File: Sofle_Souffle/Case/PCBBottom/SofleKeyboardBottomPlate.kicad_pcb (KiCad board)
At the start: 2 copper layers, 143.4 x 111.8 mm, 15 parts

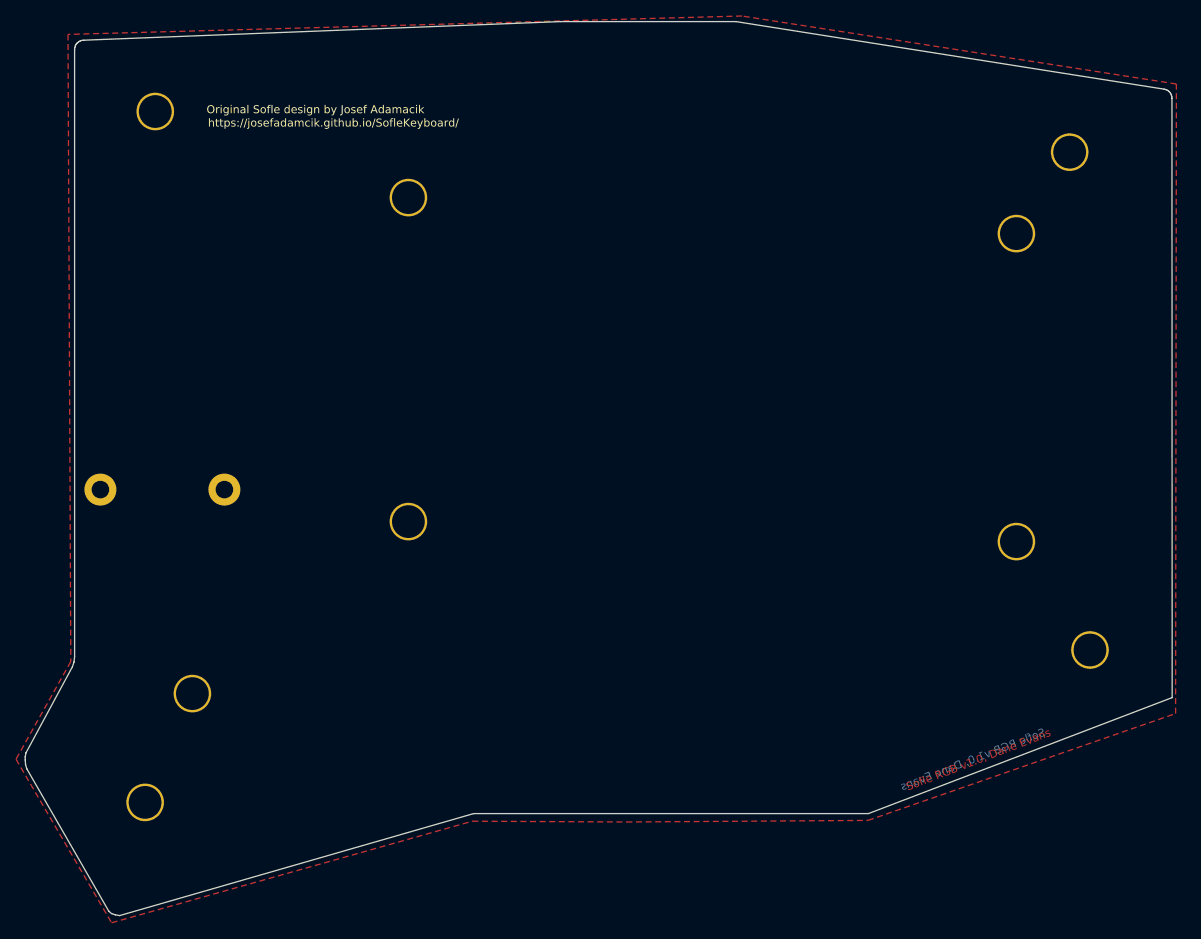
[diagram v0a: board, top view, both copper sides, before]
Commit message: Updated bottom plate and added SVG files for case creation.
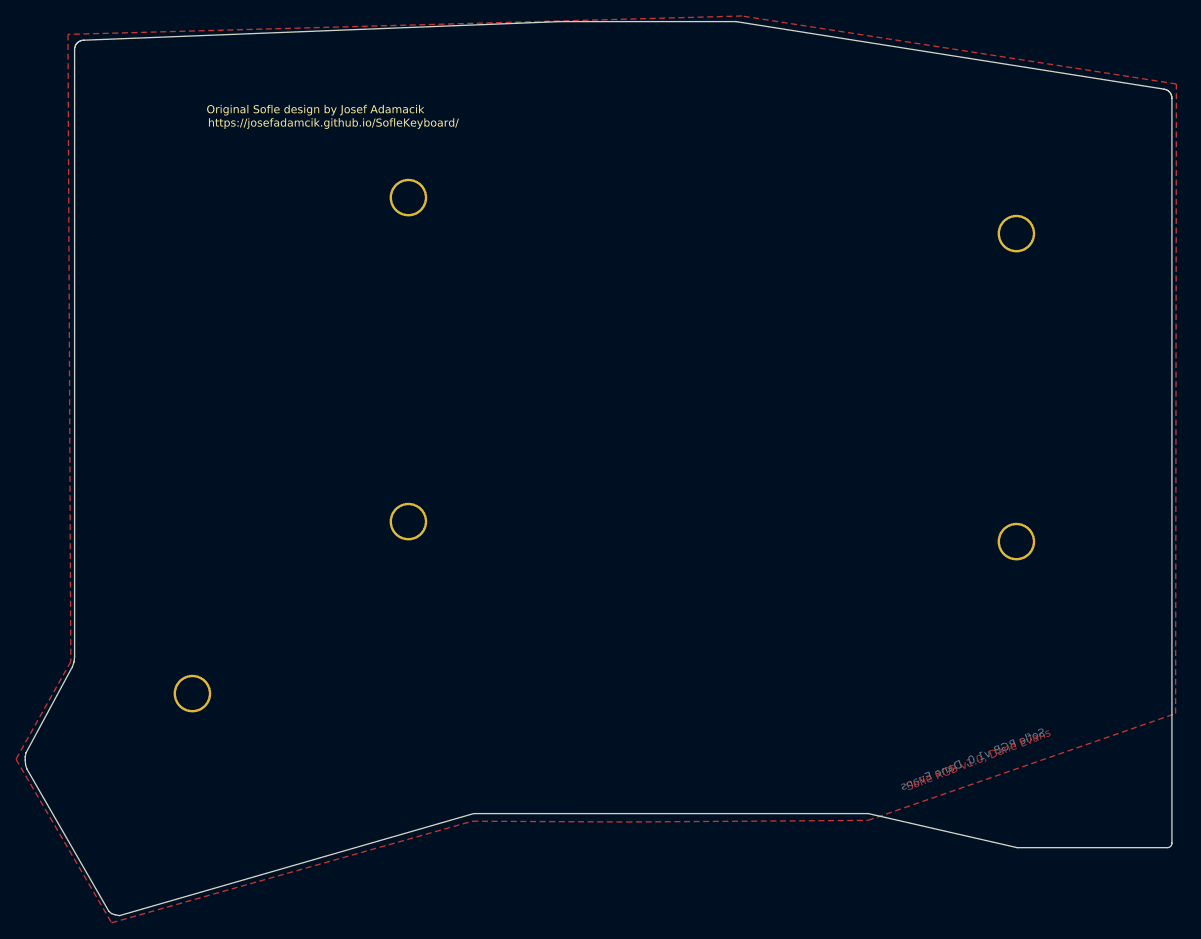
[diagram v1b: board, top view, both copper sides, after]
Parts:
- removed TH1, TH2: HOLE, SofleKeyboard-footprint:M2_HOLE_PCB
- removed the TH3 at (215.9, 114.3)
- removed the TH3 at (213.4, 52.1)
- removed the TH3 at (97.8, 133.3)
- removed the TH3 at (99.1, 47.0)
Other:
- board size 143.4 x 111.8 mm -> 143.3 x 111.8 mm
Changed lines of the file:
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@@
-(kicad_pcb (version 20171130) (host pcbnew "(5.1.6)-1")
+(kicad_pcb (version 20171130) (host pcbnew "(5.1.12-1-10_14)")
   (general
     (thickness 1.6)
-    (drawings 41)
+    (drawings 44)
     (tracks 0)
     (zones 0)
-    (modules 15)
+    (modules 9)
     (nets 1)
   )
@@
     (38 B.Mask user)
     (39 F.Mask user)
-    (40 Dwgs.User user hide)
+    (40 Dwgs.User user)
     (41 Cmts.User user hide)
     (42 Eco1.User user hide)
@@
   )
   (module SofleKeyboard-footprint:HOLE_M2_TH (layer F.Cu)
-    (at 215.9 114.3)
-    (fp_text reference TH3 (at 0 -2.54) (layer F.SilkS) hide
-      (effects (font (size 0.29972 0.29972) (thickness 0.0762)))
-    )
-    (fp_text value HOLE (at 0 2.54) (layer F.SilkS) hide
-      (effects (font (size 0.29972 0.29972) (thickness 0.0762)))
-    )
-    (pad "" thru_hole circle (at 0.025 -0.075 90) (size 4.7 4.7) (drill 4.1) (layers *.Cu *.Mask Dwgs.User)
-      (clearance 0.3))
-  )
-  (module SofleKeyboard-footprint:HOLE_M2_TH (layer F.Cu)
-    (at 213.36 52.07)
-    (fp_text reference TH3 (at 0 -2.54) (layer F.SilkS) hide
-      (effects (font (size 0.29972 0.29972) (thickness 0.0762)))
-    )
-    (fp_text value HOLE (at 0 2.54) (layer F.SilkS) hide
-      (effects (font (size 0.29972 0.29972) (thickness 0.0762)))
-    )
-    (pad "" thru_hole circle (at 0.025 -0.075 90) (size 4.7 4.7) (drill 4.1) (layers *.Cu *.Mask Dwgs.User)
-      (clearance 0.3))
-  )
-  (module SofleKeyboard-footprint:HOLE_M2_TH (layer F.Cu)
-    (at 97.79 133.35)
-    (fp_text reference TH3 (at 0 -2.54) (layer F.SilkS) hide
-      (effects (font (size 0.29972 0.29972) (thickness 0.0762)))
-    )
-    (fp_text value HOLE (at 0 2.54) (layer F.SilkS) hide
-      (effects (font (size 0.29972 0.29972) (thickness 0.0762)))
-    )
-    (pad "" thru_hole circle (at 0.025 -0.075 90) (size 4.7 4.7) (drill 4.1) (layers *.Cu *.Mask Dwgs.User)
-      (clearance 0.3))
-  )
-  (module SofleKeyboard-footprint:HOLE_M2_TH (layer F.Cu)
-    (at 99.06 46.99)
-    (fp_text reference TH3 (at 0 -2.54) (layer F.SilkS) hide
-      (effects (font (size 0.29972 0.29972) (thickness 0.0762)))
-    )
-    (fp_text value HOLE (at 0 2.54) (layer F.SilkS) hide
-      (effects (font (size 0.29972 0.29972) (thickness 0.0762)))
-    )
-    (pad "" thru_hole circle (at 0.025 -0.075 90) (size 4.7 4.7) (drill 4.1) (layers *.Cu *.Mask Dwgs.User)
-      (clearance 0.3))
-  )
-  (module SofleKeyboard-footprint:M2_HOLE_PCB (layer F.Cu)
-    (at 92.225 94.175)
-    (fp_text reference TH1 (at 0 2.7) (layer F.SilkS) hide
-      (effects (font (size 1 1) (thickness 0.15)))
-    )
-    (fp_text value HOLE (at 0 -2.6) (layer F.Fab)
-      (effects (font (size 1 1) (thickness 0.15)))
-    )
-    (pad "" thru_hole circle (at 0 0) (size 4 4) (drill 2.2) (layers *.Cu *.Mask Dwgs.User))
-  )
-  (module SofleKeyboard-footprint:HOLE_M2_TH (layer F.Cu)
     (at 206.9 100.7)
     (fp_text reference TH6 (at 0 -2.54) (layer F.SilkS) hide
@@
       (clearance 0.3))
   )
-  (module SofleKeyboard-footprint:M2_HOLE_PCB (layer F.Cu)
-    (at 107.725 94.175)
-    (fp_text reference TH2 (at 0 2.7) (layer F.SilkS) hide
-      (effects (font (size 1 1) (thickness 0.15)))
-    )
-    (fp_text value HOLE (at 0 -2.6) (layer F.Fab)
-      (effects (font (size 1 1) (thickness 0.15)))
-    )
-    (pad "" thru_hole circle (at 0 0) (size 4 4) (drill 2.2) (layers *.Cu *.Mask Dwgs.User))
-  )
   (module SofleKeyboard-footprint:HOLE_M2_TH (layer F.Cu)
     (at 130.7 57.75)
@@
       (clearance 0.3))
   )
+  (dimension 143.332205 (width 0.15) (layer Dwgs.User)
+    (gr_text "143.332 mm" (at 154.502641 154.720359 0.01523013774) (layer Dwgs.User)
+      (effects (font (size 1 1) (thickness 0.15)))
+    )
+    (feature1 (pts (xy 226.1616 127.8382) (xy 226.168551 153.98773)))
+    (feature2 (pts (xy 82.8294 127.8763) (xy 82.836351 154.02583)))
+    (crossbar (pts (xy 82.836195 153.439409) (xy 226.168395 153.401309)))
+    (arrow1a (pts (xy 226.168395 153.401309) (xy 225.042047 153.988029)))
+    (arrow1b (pts (xy 226.168395 153.401309) (xy 225.041735 152.815188)))
+    (arrow2a (pts (xy 82.836195 153.439409) (xy 83.962855 154.02553)))
+    (arrow2b (pts (xy 82.836195 153.439409) (xy 83.962543 152.852689)))
+  )
+  (gr_line (start 225.592641 138.932819) (end 206.8322 138.93282) (layer Edge.Cuts) (width 0.1))
+  (gr_arc (start 225.59772 138.36386) (end 225.592641 138.932819) (angle -90.5) (layer Edge.Cuts) (width 0.1))
+  (gr_line (start 226.168181 45.256902) (end 226.166702 138.363974) (layer Edge.Cuts) (width 0.1))
+  (gr_line (start 206.8322 138.93282) (end 188.2219 134.673) (layer Edge.Cuts) (width 0.1))
+  (gr_line (start 138.879128 134.675) (end 188.2219 134.673) (layer Edge.Cuts) (width 0.1))
   (gr_text "Original Sofle design by Josef Adamacik" (at 119.105 48.585) (layer B.SilkS)
     (effects (font (size 1 1) (thickness 0.2)) (justify mirror))
@@
   (gr_line (start 89.19559 38.508327) (end 89.336259 38.337831) (layer Edge.Cuts) (width 0.1))
   (gr_line (start 83.025 129.075) (end 82.875 128.575) (layer Edge.Cuts) (width 0.1))
-  (gr_line (start 138.879128 134.675) (end 188.225 134.675) (layer Edge.Cuts) (width 0.1))
   (gr_line (start 149.725 35.675) (end 90.150853 38.000405) (layer Edge.Cuts) (width 0.1))
   (gr_line (start 226.095281 44.853672) (end 226.149381 45.049571) (layer Edge.Cuts) (width 0.1))
@@
   (gr_line (start 82.925 127.075) (end 88.725 116.325) (layer Edge.Cuts) (width 0.1))
   (gr_line (start 226.149381 45.049571) (end 226.168181 45.256902) (layer Edge.Cuts) (width 0.1))
-  (gr_line (start 226.168181 45.256902) (end 226.195181 120.175) (layer Edge.Cuts) (width 0.1))
   (gr_line (start 225.200441 44.120146) (end 225.402111 44.171776) (layer Edge.Cuts) (width 0.1))
   (gr_line (start 93.275 146.875) (end 93.625 147.175) (layer Edge.Cuts) (width 0.1))
@@
   (gr_line (start 88.998857 39.152435) (end 89.022257 38.920261) (layer Edge.Cuts) (width 0.1))
   (gr_line (start 89.022257 38.920261) (end 89.089377 38.704014) (layer Edge.Cuts) (width 0.1))
-  (gr_line (start 226.195181 120.175) (end 188.225 134.675) (layer Edge.Cuts) (width 0.15))
   (gr_line (start 225.402111 44.171776) (end 225.586871 44.256466) (layer Edge.Cuts) (width 0.1))
   (gr_line (start 93.625 147.175) (end 94.075 147.325) (layer Edge.Cuts) (width 0.1))

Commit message: Corrected bottom plate.
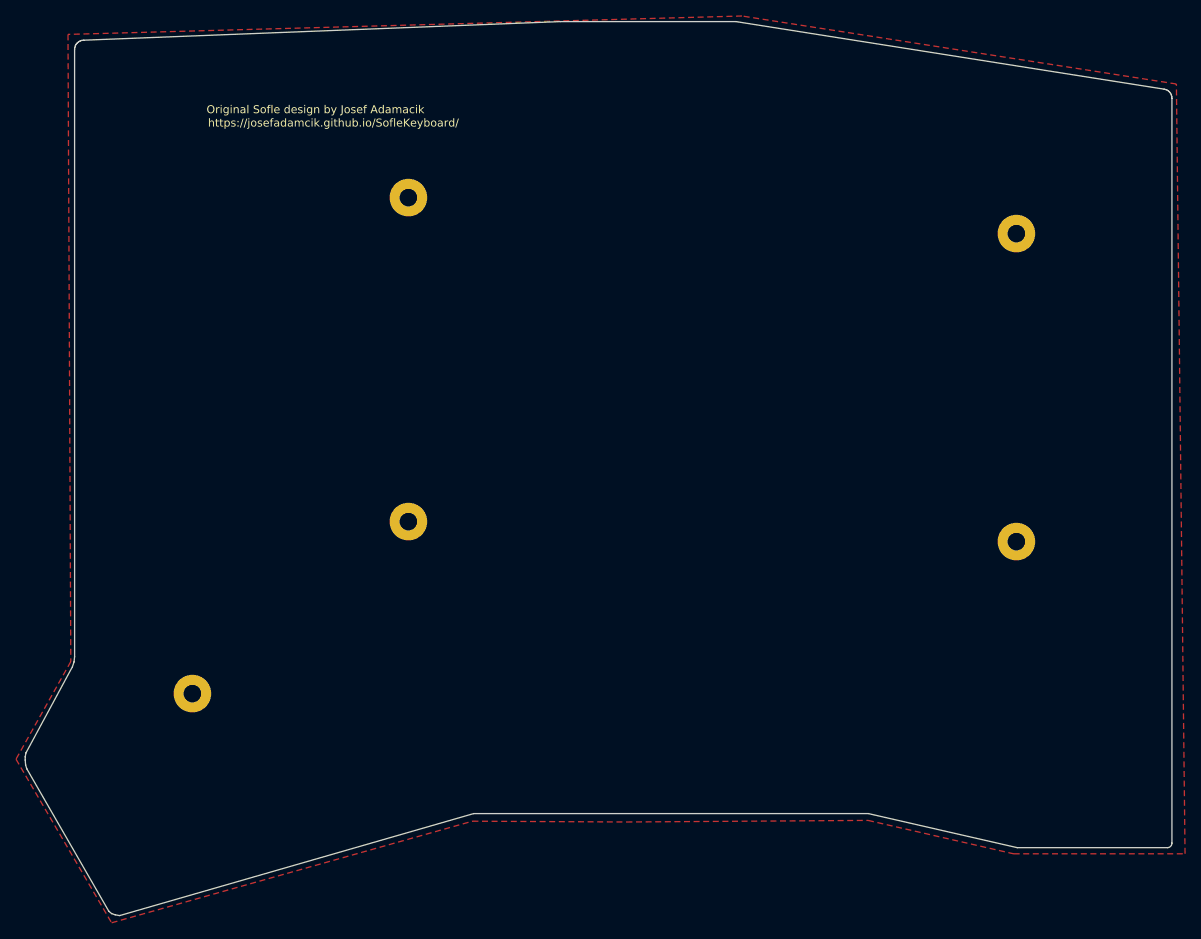
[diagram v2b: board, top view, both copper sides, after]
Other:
- net class Default removed
- board text removed: "Sofle RGB v1.0, Dane Evans"

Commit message: Case updates.
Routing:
- added copper zone on B.Cu, net (none)
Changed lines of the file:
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@@
     (style (thickness 0.15) (arrow_length 1.27) (text_position_mode 0) (extension_height 0.58642) (extension_offset 0) keep_text_aligned)
   )
-  (zone (net 0) (net_name "") (layer "F.Cu") (hatch edge 0.508)
+  (zone (net 0) (net_name "") (layers F&B.Cu) (hatch edge 0.508)
     (connect_pads (clearance 0.508))
     (min_thickness 0.254) (filled_areas_thickness no)
